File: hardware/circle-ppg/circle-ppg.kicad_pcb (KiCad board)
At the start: 4 copper layers, 25 x 18 mm, 11 parts

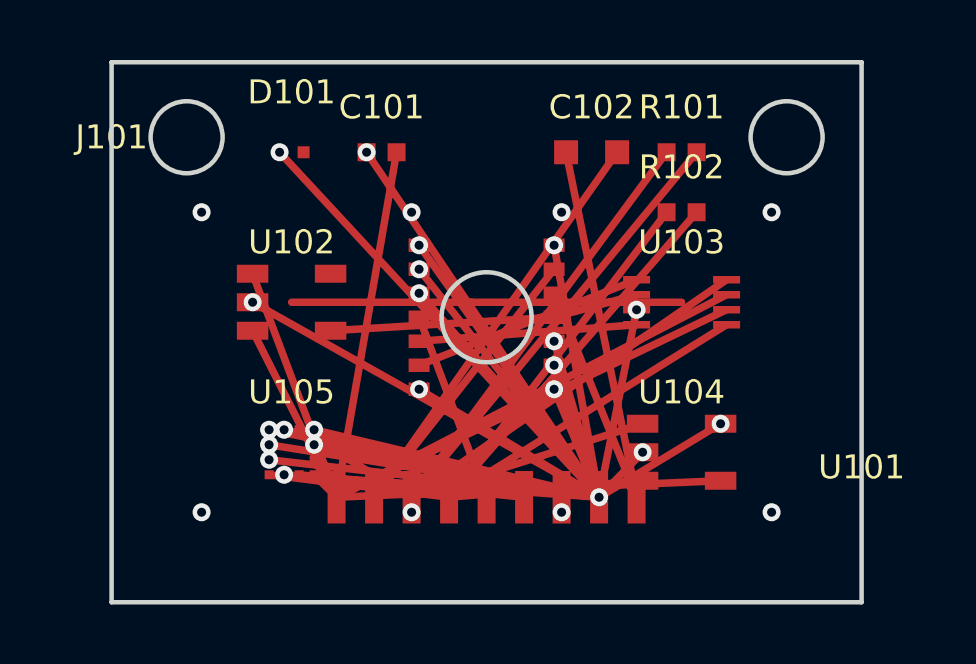
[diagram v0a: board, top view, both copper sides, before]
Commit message: hardware: resolve all DRC violations down to 0 on main and ppg boards
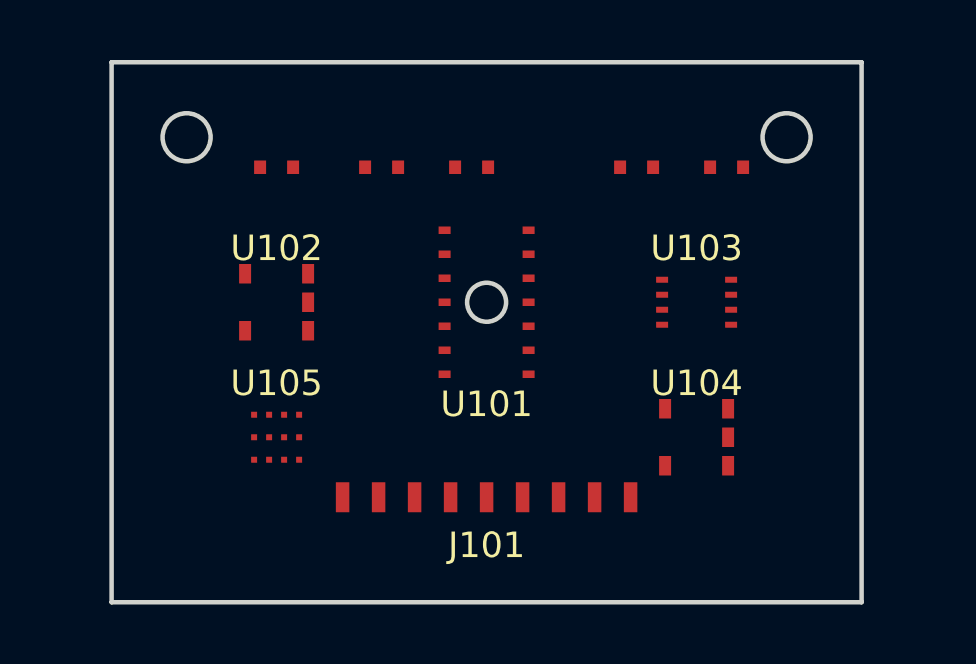
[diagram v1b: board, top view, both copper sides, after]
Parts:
- C101: value (none) -> 1.0uF; footprint Capacitor_SMD:C_0402_1005Metric -> R_0402
- C102: value (none) -> 10uF; footprint Capacitor_SMD:C_0603_1608Metric -> R_0402
- D101: value (none) -> ESD; footprint Package_TO_SOT_SMD:SOD-923 -> R_0402
- J101: value (none) -> PPG_HEAD; footprint Connector_JST:JST_GH_BM09B-GHS-TBT_1x09-1MP_P1.25mm_Vertical -> JST_GH_9P
- R101, R102: value (none) -> 33R; footprint Resistor_SMD:R_0402_1005Metric -> R_0402
- U101: value (none) -> MAX30102; footprint Sensor_Optical:Maxim_OLGA-14_3.3x5.6mm_P0.8mm -> OLGA-14
- U102: value (none) -> LP5907MFX-1.8; footprint Package_TO_SOT_SMD:SOT-23-5 -> SOT-23-5
- U103: value (none) -> TXS0102DCUR; footprint Package_SO:VSSOP-8_2.3x2mm_P0.5mm -> VSSOP-8
- U104: value (none) -> AT24CS02; footprint Package_TO_SOT_SMD:SOT-23-5 -> SOT-23-5
- U105: value (none) -> LIS2DW12; footprint Package_LGA:LGA-12_2x2mm_P0.5mm -> LGA-12
- moved C102 4.03 mm to (12.0, 3.50)
- moved R102 2.12 mm to (20.5, 3.50)
- moved R101 1.58 mm to (17.5, 3.50)
- moved D101 0.71 mm to (5.50, 3.50)
- moved U104 0.71 mm to (19.5, 12.5)
- moved U105 0.71 mm to (5.50, 12.5)
- moved C101 0.50 mm to (9.00, 3.50)
- moved U101 0.50 mm to (12.5, 8.00)
- moved U102 0.50 mm to (5.50, 8.00)
- moved U103 0.50 mm to (19.5, 8.00)
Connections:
- C101 pad 1: PPG_LOGIC_GND -> PPG_1V8
- C101 pad 2: PPG_3V3 -> PPG_LOGIC_GND
- C102 pad 1: PPG_LED_GND -> PPG_LED_PWR
- C102 pad 2: PPG_LED_PWR -> PPG_LED_GND
- D101 pad 1: PPG_LOGIC_GND -> PPG_3V3
- D101 pad 2: (no net) -> PPG_LOGIC_GND
- U101 pad 10: PPG_LED_GND -> PPG_LED_PWR
- U101 pad 11: PPG_1V8 -> PPG_LED_GND
- U101 pad 12: PPG_LOGIC_GND -> PPG_LED_GND
- U101 pad 13: PPG_LOGIC_GND -> PPG_LED_GND
- U101 pad 2: PPG_SDA_1V8 -> PPG_1V8
- U101 pad 3: PPG_SCL_1V8 -> PPG_1V8
- U101 pad 4: PPG_INT -> PPG_SDA_1V8
- U101 pad 5: PPG_LOGIC_GND -> PPG_SCL_1V8
- U101 pad 6: PPG_LOGIC_GND -> PPG_INT
- U101 pad 9: PPG_LED_PWR -> PPG_LOGIC_GND
- U102 pad 4: (no net) -> PPG_LOGIC_GND
- U103 pad 1: PPG_SCL_1V8 -> PPG_1V8
- U103 pad 2: PPG_LOGIC_GND -> PPG_SDA_1V8
- U103 pad 3: PPG_1V8 -> PPG_SCL_1V8
- U103 pad 4: PPG_SDA_1V8 -> PPG_LOGIC_GND
- U103 pad 5: PPG_SDA_3V3 -> PPG_3V3
- U103 pad 6: PPG_3V3 -> PPG_SCL_3V3
- U103 pad 7: PPG_3V3 -> PPG_SDA_3V3
- U103 pad 8: PPG_SCL_3V3 -> PPG_3V3
- U105 pad 1: PPG_SCL_3V3 -> PPG_LOGIC_GND
- U105 pad 10: PPG_3V3 -> PPG_LOGIC_GND
- U105 pad 11: PPG_MOTION_INT -> PPG_LOGIC_GND
- U105 pad 6: PPG_SDA_3V3 -> PPG_LOGIC_GND
- U105 pad 9: PPG_3V3 -> PPG_LOGIC_GND
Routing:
- net PPG_LOGIC_GND: track 188.7 -> 0.00 mm, vias 30 -> 0
- net PPG_3V3: track 70.3 -> 0.00 mm
- net PPG_SDA_3V3: track 54.4 -> 0.00 mm
- net PPG_SCL_3V3: track 47.9 -> 0.00 mm
- net PPG_LED_PWR: track 23.7 -> 0.00 mm
- net PPG_1V8: track 23.3 -> 0.00 mm
- net PPG_LED_GND: track 19.1 -> 0.00 mm
- net PPG_SDA_1V8: track 7.79 -> 0.00 mm
- net PPG_MOTION_INT: track 7.54 -> 0.00 mm
- net PPG_SCL_1V8: track 7.27 -> 0.00 mm
- net PPG_INT: track 6.41 -> 0.00 mm
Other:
- outline, holes or cut-outs redrawn
- rule pad_to_mask_clearance: 0.05 -> 0.02
- rule solder_mask_min_width: 0.1 -> 0.04
